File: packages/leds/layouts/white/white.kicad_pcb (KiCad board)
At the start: 2 copper layers, 2 parts, among them U1 2.85V

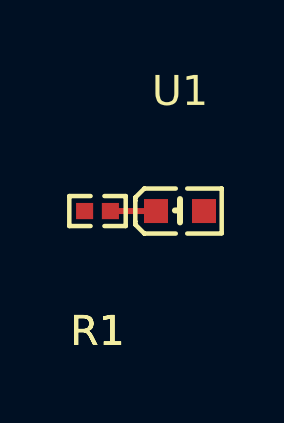
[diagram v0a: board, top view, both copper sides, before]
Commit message: rebuild all packages & regenerate images of changed layouts (silk)
Add new scripts for version bump and build (based on atopile/packages)
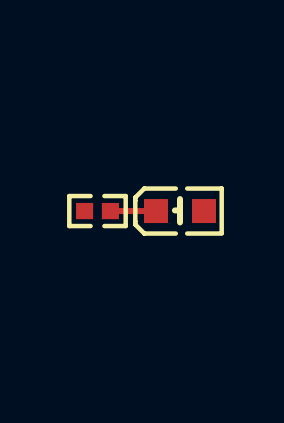
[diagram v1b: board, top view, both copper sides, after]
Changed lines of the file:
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@@
             (at 0 -4 0)
             (layer "F.SilkS")
-            (hide no)
+            (hide yes)
             (effects
                 (font
@@
             )
         )
-        (property "checksum" "1e8332dfb37f08afa2745e8e7e35ba43ce14b96f2d713ec34573933eb878ecf4"
+        (property "checksum" "ff436f6108697cce0f2f1866a5d168e4baf057c8764c3b46685c1d1c6ab2697e"
             (at 0 0 0)
             (layer "User.9")
@@
             )
         )
-        (property "__atopile_lib_fp_hash__" "231b01ed-b381-648e-2769-ae4396f0859a"
+        (property "__atopile_lib_fp_hash__" "675507c7-7f42-68de-b7a7-fdfa83c2e195"
             (at 0 0 0)
             (layer "User.9")
@@
                     (thickness 0.15)
                 )
+                (hide yes)
             )
             (unlocked no)
@@
             (at 0 -4 0)
             (layer "F.SilkS")
-            (hide no)
+            (hide yes)
             (effects
                 (font
@@
                     (thickness 0.15)
                 )
+                (hide yes)
             )
             (unlocked no)
@@
                     (thickness 0.15)
                 )
+                (hide yes)
             )
             (unlocked no)
